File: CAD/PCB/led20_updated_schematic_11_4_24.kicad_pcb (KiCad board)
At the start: 2 copper layers, 7 parts

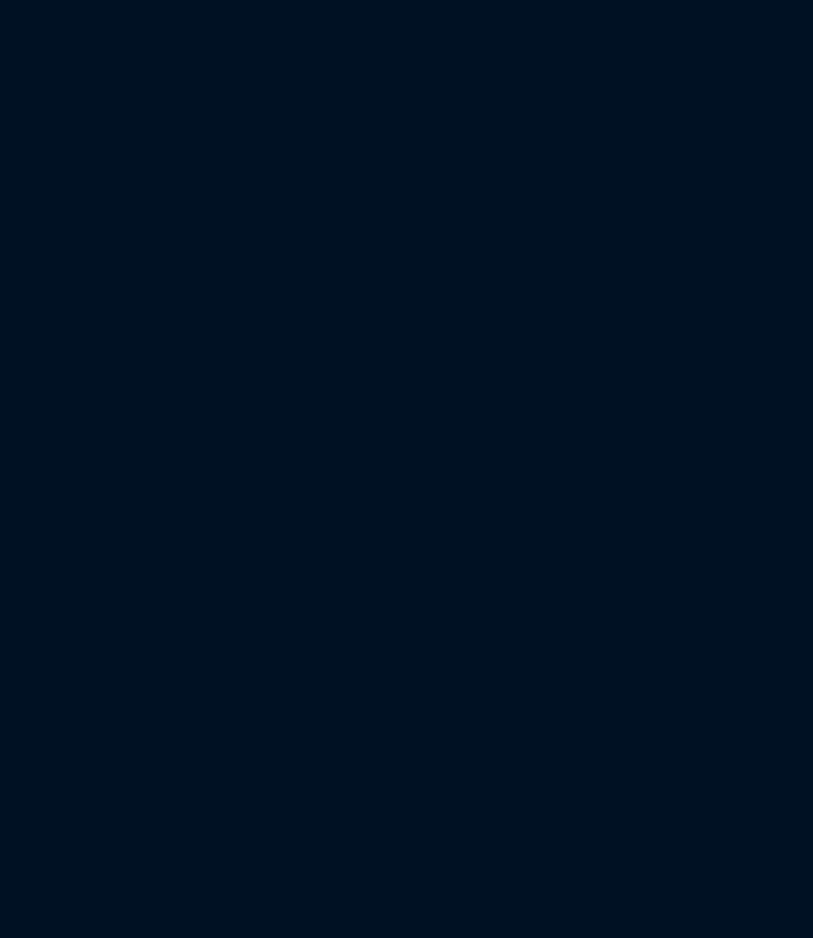
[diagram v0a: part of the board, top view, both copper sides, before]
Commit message: Updated PCB
Added esp32 footprint
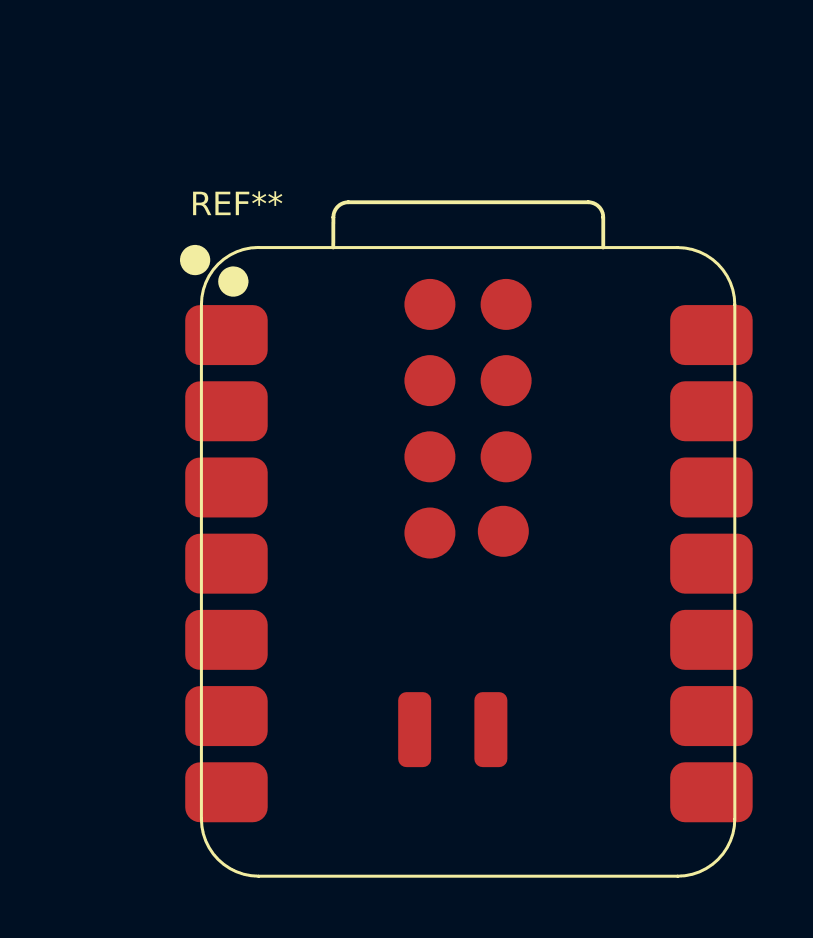
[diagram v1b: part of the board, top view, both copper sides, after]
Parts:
- added REF**: XIAO-ESP32-C6-SMD, Led20:XIAO-ESP32-C6-SMD, F.Cu at (207.0, 97.0)

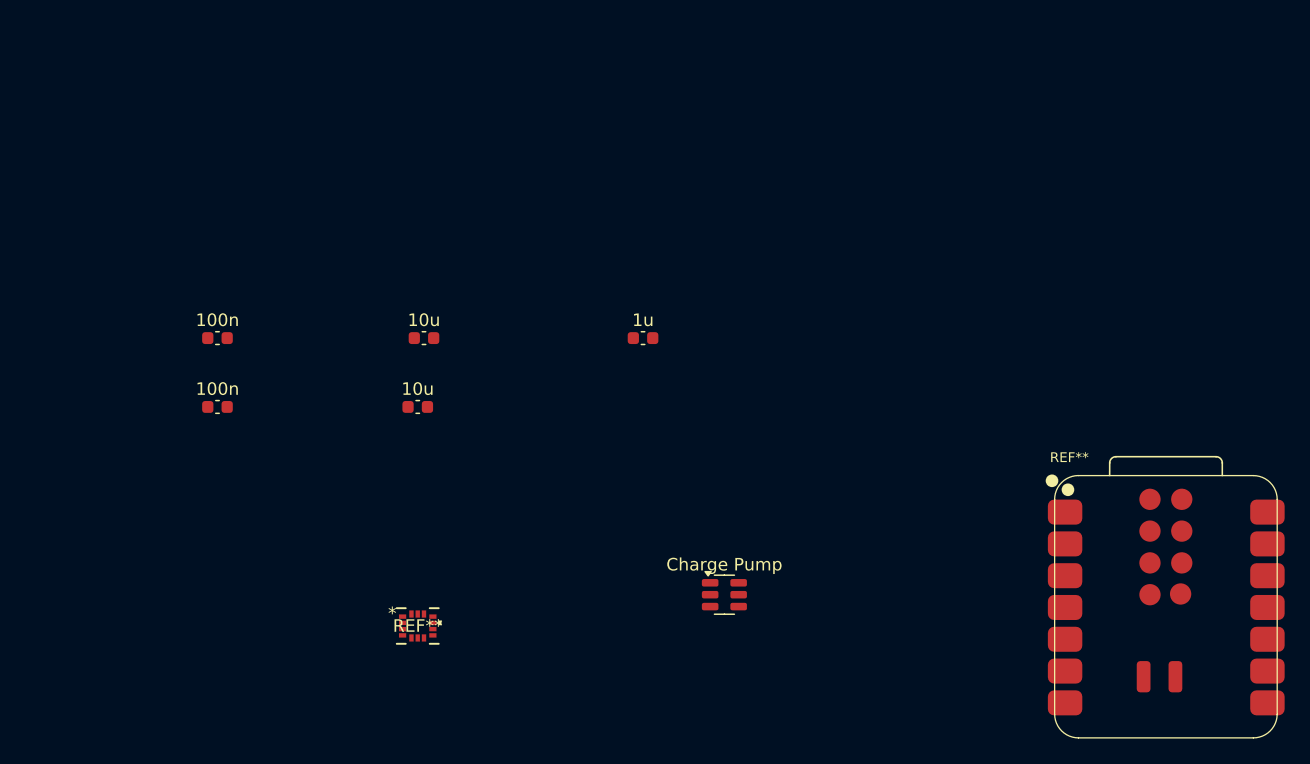
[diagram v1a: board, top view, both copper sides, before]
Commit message: Updated PCB
Pins for Microcontroller on schematic had to be changed to reflect the footprint pin out. This may need closer attention for all ICs, i'll double check that tomorrow. Also found connector for battery. Changed battery symbol in schematic to avoid errors. LED array was combined to make one 20 LED array instead of two seperate 10 LED arrays. Points for wireless charging still need to be added to both schematic and PCB
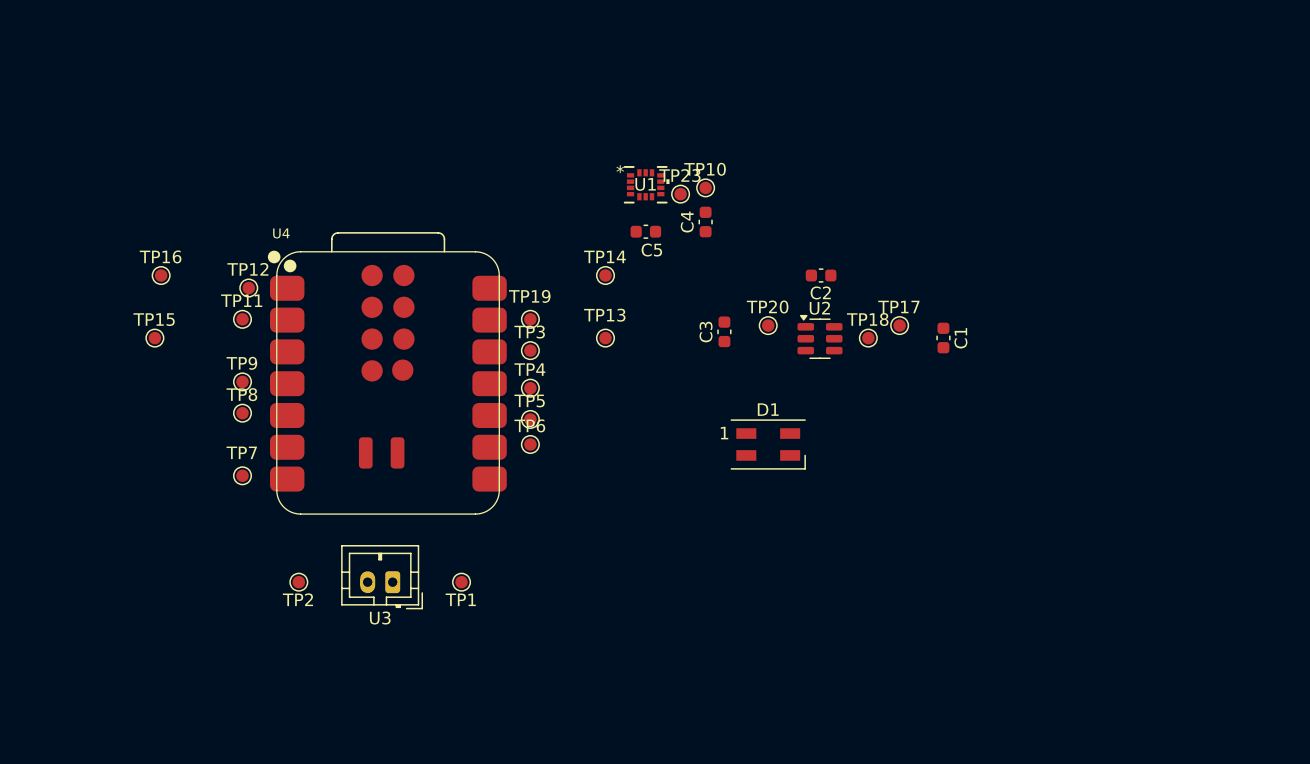
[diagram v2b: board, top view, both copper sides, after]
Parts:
- removed 100n (x2), 10u (x2), 1u: C_0603_1608Metric, Capacitor_SMD:C_0603_1608Metric
- removed Charge Pump: ChargePump, Led20:ChargePump
- removed REF**: LGA-14L_2P5X3X0P83_STM, Led20:LGA-14L_2P5X3X0P83_STM-L
- removed REF**: XIAO-ESP32-C6-SMD, Led20:XIAO-ESP32-C6-SMD
- added C1: 1u, Capacitor_SMD:C_0603_1608Metric, F.Cu at (189.0, 75.5)
- added C2: 10u, Capacitor_SMD:C_0603_1608Metric, F.Cu at (179.2, 70.5)
- added C3: 10u, Capacitor_SMD:C_0603_1608Metric, F.Cu at (171.5, 75.0)
- added C4: 100n, Capacitor_SMD:C_0603_1608Metric, F.Cu at (170.0, 66.2)
- added C5: 100n, Capacitor_SMD:C_0603_1608Metric, F.Cu at (165.2, 67.0)
- added D1: SK6812MINI, LED_SMD:LED_SK6812MINI_PLCC4_3.5x3.5mm_P1.75mm, F.Cu at (175.0, 84.0)
- added TP1: ~, TestPoint:TestPoint_Pad_D1.0mm, F.Cu at (150.5, 95.0)
- added TP10: ~, TestPoint:TestPoint_Pad_D1.0mm, F.Cu at (170.0, 63.5)
- added TP11: ~, TestPoint:TestPoint_Pad_D1.0mm, F.Cu at (133.0, 74.0)
- added TP12: ~, TestPoint:TestPoint_Pad_D1.0mm, F.Cu at (133.5, 71.5)
- added TP13: ~, TestPoint:TestPoint_Pad_D1.0mm, F.Cu at (162.0, 75.5)
- added TP14: ~, TestPoint:TestPoint_Pad_D1.0mm, F.Cu at (162.0, 70.5)
- added TP15: ~, TestPoint:TestPoint_Pad_D1.0mm, F.Cu at (126.0, 75.5)
- added TP16: ~, TestPoint:TestPoint_Pad_D1.0mm, F.Cu at (126.5, 70.5)
- added TP17: ~, TestPoint:TestPoint_Pad_D1.0mm, F.Cu at (185.5, 74.5)
- added TP18: ~, TestPoint:TestPoint_Pad_D1.0mm, F.Cu at (183.0, 75.5)
- added TP19: ~, TestPoint:TestPoint_Pad_D1.0mm, F.Cu at (156.0, 74.0)
- added TP2: ~, TestPoint:TestPoint_Pad_D1.0mm, F.Cu at (137.5, 95.0)
- added TP20: ~, TestPoint:TestPoint_Pad_D1.0mm, F.Cu at (175.0, 74.5)
- added TP23: ~, TestPoint:TestPoint_Pad_D1.0mm, F.Cu at (168.0, 64.0)
- added TP3: ~, TestPoint:TestPoint_Pad_D1.0mm, F.Cu at (156.0, 76.5)
- added TP4: ~, TestPoint:TestPoint_Pad_D1.0mm, F.Cu at (156.0, 79.5)
- added TP5: ~, TestPoint:TestPoint_Pad_D1.0mm, F.Cu at (156.0, 82.0)
- added TP6: ~, TestPoint:TestPoint_Pad_D1.0mm, F.Cu at (156.0, 84.0)
- added TP7: ~, TestPoint:TestPoint_Pad_D1.0mm, F.Cu at (133.0, 86.5)
- added TP8: ~, TestPoint:TestPoint_Pad_D1.0mm, F.Cu at (133.0, 81.5)
- added TP9: ~, TestPoint:TestPoint_Pad_D1.0mm, F.Cu at (133.0, 79.0)
- added U1: ~, Led20:LGA-14L_2P5X3X0P83_STM-L, F.Cu at (165.2, 63.2)
- added U2: ~, Led20:ChargePump, F.Cu at (179.1, 75.5)
- added U3: Battery, Connector_JST:JST_PH_B2B-PH-K_1x02_P2.00mm_Vertical, F.Cu at (145.0, 95.0)
- added U4: ~, Led20:XIAO-ESP32-C6-SMD, F.Cu at (144.9, 79.1)

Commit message: Updated PCB and Schematic
Changed schematic to include charging contact points and double checked pinouts on ICs
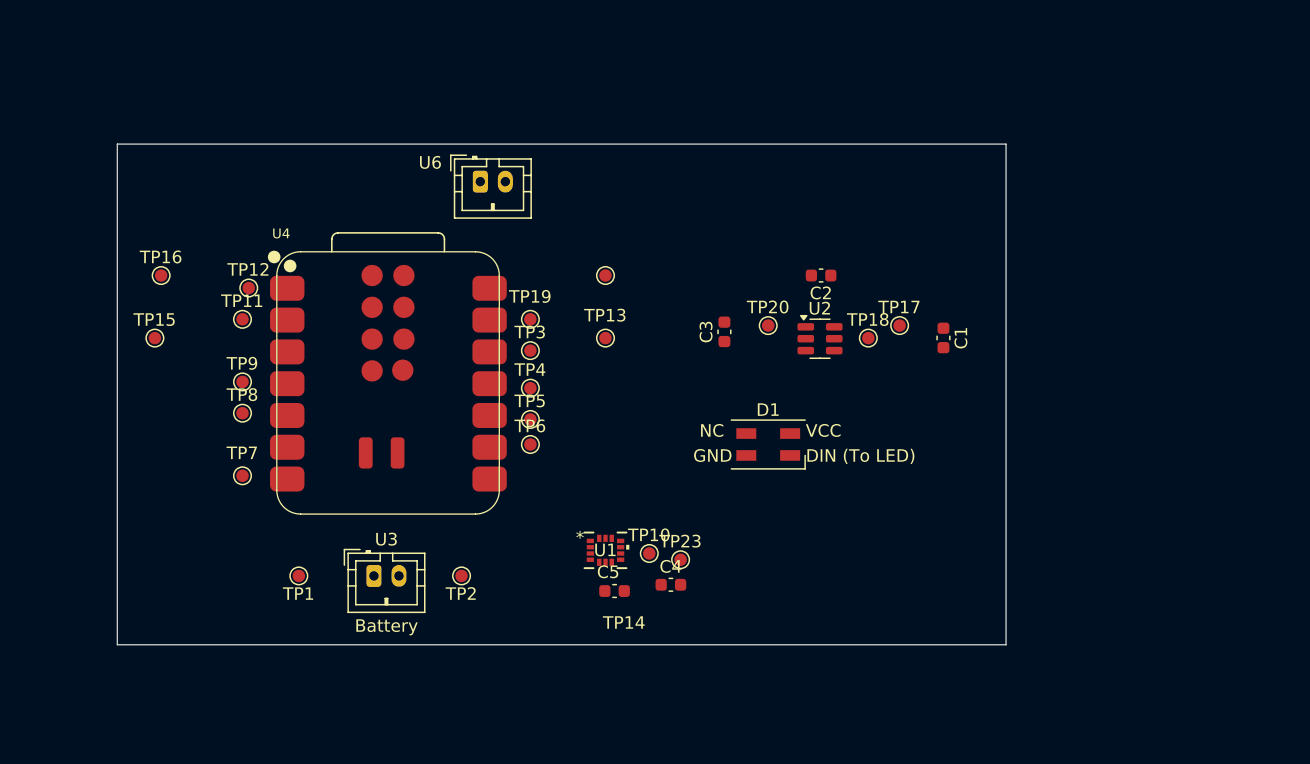
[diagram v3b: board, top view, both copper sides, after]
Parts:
- added U6: JST, Connector_JST:JST_PH_B2B-PH-K_1x02_P2.00mm_Vertical, F.Cu at (152.0, 63.0)
- moved TP10 29.6 mm to (165.5, 92.7)
- moved U1 29.4 mm to (162.0, 92.5)
- moved TP23 29.2 mm to (168.0, 93.2)
- moved C4 29.1 mm to (167.2, 95.2), turned to 0 degrees
- moved C5 28.8 mm to (162.7, 95.7), turned to 0 degrees
- moved TP1 13.0 mm to (137.5, 94.5)
- moved TP2 13.0 mm to (150.5, 94.5)
- moved U3 1.58 mm to (143.5, 94.5), turned to 0 degrees
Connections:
- U4 pad 14: unconnected-(U4-5V-Pad14) -> +5V IN
- U4 pad 15: GND -> VBATT
- U4 pad 16: VBATT -> GND
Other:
- board outline added: 71 x 40 mm
- board text added: "DIN (To LED)"
- board text added: "GND"
- board text added: "NC"
- board text added: "VCC"

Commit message: Updated PCB and Schematic
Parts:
- added BZ1: Piezo Buzzer, Buzzer_Beeper:Buzzer_12x9.5RM7.6, F.Cu at (163.6, 90.0)
- moved C1 24.7 mm to (165.6, 67.5)
- moved TP17 23.8 mm to (163.1, 66.5)
- moved TP18 23.3 mm to (161.1, 67.5)
- moved C2 23.0 mm to (157.7, 62.5)
- moved C3 23.0 mm to (150.0, 67.0)
- moved TP20 23.0 mm to (153.5, 66.5)
- moved U2 23.0 mm to (157.6, 67.5)
- moved TP13 19.7 mm to (146.0, 64.0)
- moved TP14 19.6 mm to (143.5, 64.0)
- moved C5 18.6 mm to (144.2, 97.3)
- moved TP10 17.8 mm to (147.7, 93.5)
- moved U1 17.8 mm to (144.2, 93.2)
- moved D1 17.7 mm to (158.0, 79.0)
- moved C4 17.0 mm to (150.2, 96.3)
- moved U6 14.6 mm to (137.5, 61.0)
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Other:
- board size 71 x 40 mm -> 55 x 55 mm
